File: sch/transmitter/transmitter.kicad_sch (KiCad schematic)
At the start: 22 parts, among them J1 VCC, J2 VCC, J3 GND, J4 GND, J5 sck_tx, J6 mosi_tx, J7 driver_in, J8 driver_ena, Q1 2N7002, U1 74HCT86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

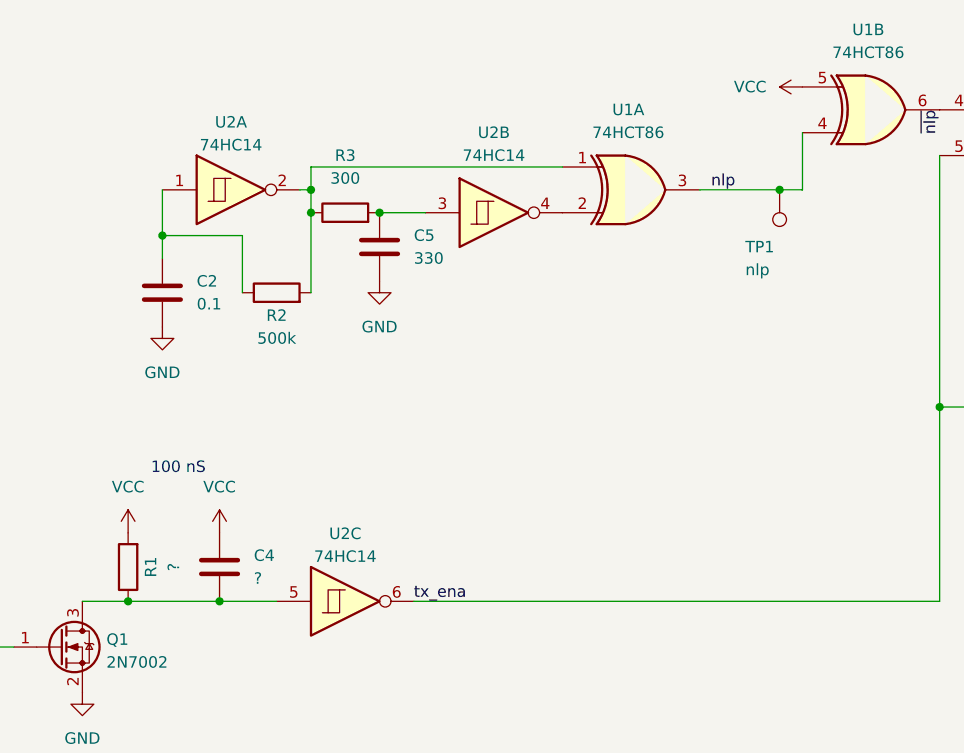
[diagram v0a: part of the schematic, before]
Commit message: Fix NLP polarity
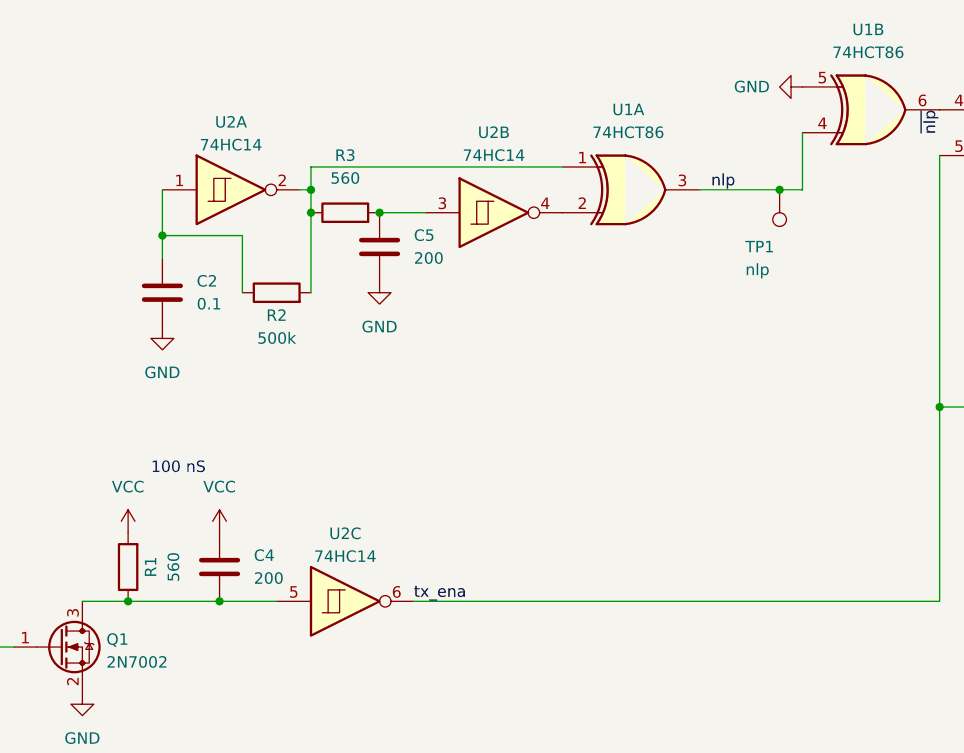
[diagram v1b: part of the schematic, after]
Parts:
- C2: footprint Capacitor_SMD:C_0805_2012Metric -> Capacitor_THT:C_Disc_D4.3mm_W1.9mm_P5.00mm
- C4: value ? -> 200
- C5: value 330 -> 200
- R1: value ? -> 560
- R3: value 300 -> 560
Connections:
- net GND: now also U1.5
- net VCC: no longer U1.5
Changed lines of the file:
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@@
     (in_bom yes) (on_board yes)
     (property "Reference" "R1" (id 0) (at 93.98 82.55 90))
-    (property "Value" "?" (id 1) (at 96.52 82.55 90))
+    (property "Value" "560" (id 1) (at 96.52 82.55 90))
     (property "Footprint" "Resistor_SMD:R_0805_2012Metric" (id 2) (at 93.218 82.55 90)
       (effects (font (size 1.27 1.27)) hide)
@@
       (effects (font (size 1.27 1.27)) (justify left))
     )
-    (property "Value" "?" (id 1) (at 105.41 83.8199 0)
+    (property "Value" "200" (id 1) (at 105.41 83.8199 0)
       (effects (font (size 1.27 1.27)) (justify left))
     )
@@
       (effects (font (size 1.27 1.27)) (justify left))
     )
-    (property "Footprint" "Capacitor_SMD:C_0805_2012Metric" (id 2) (at 96.2152 55.88 0)
+    (property "Footprint" "Capacitor_THT:C_Disc_D4.3mm_W1.9mm_P5.00mm" (id 2) (at 96.2152 55.88 0)
       (effects (font (size 1.27 1.27)) hide)
     )
@@
     (pin "1")
   )
-  (symbol (lib_id "power:VCC") (at 166.37 29.21 90) (unit 1)
-    (in_bom yes) (on_board yes)
-    (property "Reference" "#PWR020" (id 0) (at 170.18 29.21 0)
-      (effects (font (size 1.27 1.27)) hide)
-    )
-    (property "Value" "VCC" (id 1) (at 158.75 29.21 90)
-      (effects (font (size 1.27 1.27)) (justify right))
-    )
-    (property "Footprint" "" (id 2) (at 166.37 29.21 0)
-      (effects (font (size 1.27 1.27)) hide)
-    )
-    (property "Datasheet" "" (id 3) (at 166.37 29.21 0)
-      (effects (font (size 1.27 1.27)) hide)
-    )
-    (pin "1")
-  )
   (symbol (lib_id "power:GND") (at 86.36 96.52 0) (unit 1)
     (in_bom yes) (on_board yes) (fields_autoplaced)
@@
     (in_bom yes) (on_board yes) (fields_autoplaced)
     (property "Reference" "R3" (id 0) (at 115.57 36.83 90))
-    (property "Value" "300" (id 1) (at 115.57 39.37 90))
+    (property "Value" "560" (id 1) (at 115.57 39.37 90))
     (property "Footprint" "Resistor_SMD:R_0805_2012Metric" (id 2) (at 115.57 44.958 90)
       (effects (font (size 1.27 1.27)) hide)
@@
     )
     (property "Datasheet" "" (id 3) (at 85.09 189.23 0)
+      (effects (font (size 1.27 1.27)) hide)
+    )
+    (pin "1")
+  )
+  (symbol (lib_id "power:GND") (at 166.37 29.21 270) (unit 1)
+    (in_bom yes) (on_board yes)
+    (property "Reference" "#PWR?" (id 0) (at 160.02 29.21 0)
+      (effects (font (size 1.27 1.27)) hide)
+    )
+    (property "Value" "GND" (id 1) (at 158.75 29.21 90)
+      (effects (font (size 1.27 1.27)) (justify left))
+    )
+    (property "Footprint" "" (id 2) (at 166.37 29.21 0)
+      (effects (font (size 1.27 1.27)) hide)
+    )
+    (property "Datasheet" "" (id 3) (at 166.37 29.21 0)
       (effects (font (size 1.27 1.27)) hide)
     )
@@
       (effects (font (size 1.27 1.27)) (justify left))
     )
-    (property "Value" "330" (id 1) (at 123.19 48.2599 0)
+    (property "Value" "200" (id 1) (at 123.19 48.2599 0)
       (effects (font (size 1.27 1.27)) (justify left))
     )
@@
       (reference "#PWR019") (unit 1) (value "GND") (footprint "")
     )
-    (path "/e4dc485a-5561-4359-8658-d4e91bbb5c5b"
-      (reference "#PWR020") (unit 1) (value "VCC") (footprint "")
-    )
     (path "/ef2fbf38-c9fb-45a6-acd1-f76e94dcddee"
       (reference "#PWR021") (unit 1) (value "VCC") (footprint "")
@@
       (reference "#PWR0101") (unit 1) (value "VCC") (footprint "")
     )
+    (path "/fc93f898-d10d-407e-b036-d3dbd960003a"
+      (reference "#PWR?") (unit 1) (value "GND") (footprint "")
+    )
     (path "/7e5bf29a-a2e8-473d-81a4-ca8f8d5cb776"
       (reference "C1") (unit 1) (value "0.1") (footprint "Capacitor_SMD:C_0805_2012Metric")
     )
     (path "/e02cf8c3-065e-4ca2-b9f3-43aede3c30ff"
-      (reference "C2") (unit 1) (value "0.1") (footprint "Capacitor_SMD:C_0805_2012Metric")
+      (reference "C2") (unit 1) (value "0.1") (footprint "Capacitor_THT:C_Disc_D4.3mm_W1.9mm_P5.00mm")
     )
     (path "/4808c559-02f9-436f-ad5d-3fd28faba215"
@@
     )
     (path "/54223930-3e91-47fb-8533-b2640a210879"
-      (reference "C4") (unit 1) (value "?") (footprint "Capacitor_SMD:C_0805_2012Metric")
+      (reference "C4") (unit 1) (value "200") (footprint "Capacitor_SMD:C_0805_2012Metric")
     )
     (path "/feb68eb5-f52f-4f82-a427-eb21d9b4b399"
-      (reference "C5") (unit 1) (value "330") (footprint "Capacitor_SMD:C_0805_2012Metric")
+      (reference "C5") (unit 1) (value "200") (footprint "Capacitor_SMD:C_0805_2012Metric")
     )
     (path "/af59b1d1-02f4-44bf-b6e3-aa49bc7a1188"
@@
     )
     (path "/06f15111-43f1-4f1a-a2b8-f0a40cffb839"
-      (reference "R1") (unit 1) (value "?") (footprint "Resistor_SMD:R_0805_2012Metric")
+      (reference "R1") (unit 1) (value "560") (footprint "Resistor_SMD:R_0805_2012Metric")
     )
     (path "/9b94f3ca-73eb-45a0-bdf1-bba85e14f7a4"
@@
     )
     (path "/fa7ac6db-b1df-4af4-9267-98c014f9dba1"
-      (reference "R3") (unit 1) (value "300") (footprint "Resistor_SMD:R_0805_2012Metric")
+      (reference "R3") (unit 1) (value "560") (footprint "Resistor_SMD:R_0805_2012Metric")
     )
     (path "/e0473134-5eab-4a53-82b8-c8079ce09e0d"
